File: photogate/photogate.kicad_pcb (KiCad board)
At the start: 2 copper layers, 72.8 x 62.1 mm, 21 parts, among them P2 3poles LOGO, P2 Jack F SJ1-3525N

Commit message: att designe PCB
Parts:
- removed Inferior Esquerdo: MountingHole_2.2mm_M2, MountingHole:MountingHole_2.2mm_M2
- removed P2 Jack F: SJ1-3525N, MyFootprints:CUI_SJ1-3525N
- removed REF** (x3): MountingHole_2.2mm_M2, MountingHole:MountingHole_2.2mm_M2
- removed REF**: OSHW-Logo_11.4x12mm_SilkScreen, Symbol:OSHW-Logo_11.4x12mm_SilkScreen
- added Furo Central: MountingHole_2.2mm_M2, MountingHole:MountingHole_2.2mm_M2, F.Cu at (110.1, 91.4)
- added Furo Inferior1: MountingHole_2.2mm_M2, MountingHole:MountingHole_2.2mm_M2, F.Cu at (94.8, 127.0)
- added Furo Inferior2: MountingHole_2.2mm_M2, MountingHole:MountingHole_2.2mm_M2, F.Cu at (162.6, 127.0)
- added Furo Superior: MountingHole_2.2mm_M2, MountingHole:MountingHole_2.2mm_M2, F.Cu at (162.6, 81.3)
- added P2 jack: SJ1-3515N, MyFootprints:CUI_SJ1-3515N, F.Cu at (91.6, 93.1)
- added R5: 470, Resistor_THT:R_Axial_DIN0204_L3.6mm_D1.6mm_P7.62mm_Horizontal, F.Cu at (104.3, 104.3)
- C1: value 104 -> 104k; footprint Capacitor_THT:C_Disc_D5.1mm_W3.2mm_P5.00mm -> Capacitor_THT:C_Disc_D10.5mm_W5.0mm_P10.00mm
- DC-005: renamed from Jack 5V1
- GLed: renamed from Green Led
- LM393N: value LM393N_A -> LM393N1
- R1: renamed from R4; footprint Resistor_THT:R_Axial_DIN0204_L3.6mm_D1.6mm_P5.08mm_Horizontal -> Resistor_THT:R_Axial_DIN0204_L3.6mm_D1.6mm_P7.62mm_Horizontal
- R2: renamed from R3; footprint Resistor_THT:R_Axial_DIN0204_L3.6mm_D1.6mm_P5.08mm_Horizontal -> Resistor_THT:R_Axial_DIN0204_L3.6mm_D1.6mm_P7.62mm_Horizontal
- R3: renamed from R1; footprint Resistor_THT:R_Axial_DIN0204_L3.6mm_D1.6mm_P5.08mm_Horizontal -> Resistor_THT:R_Axial_DIN0204_L3.6mm_D1.6mm_P7.62mm_Horizontal
- R4: renamed from R2; footprint Resistor_THT:R_Axial_DIN0204_L3.6mm_D1.6mm_P5.08mm_Horizontal -> Resistor_THT:R_Axial_DIN0204_L3.6mm_D1.6mm_P7.62mm_Horizontal
- RLed: renamed from Red Led
- moved P2 3poles 30.0 mm to (102.0, 101.2)
- moved R4 28.5 mm to (103.5, 107.7), turned to -90 degrees
- moved C1 22.8 mm to (119.4, 109.7), turned to -90 degrees
- moved R2 21.8 mm to (125.5, 79.5)
- moved DC-005 21.1 mm to (96.0, 77.7)
- moved VR1 18.9 mm to (94.6, 112.8), turned to -90 degrees
- moved R1 13.3 mm to (136.8, 79.5)
- moved R3 13.3 mm to (107.0, 78.7), turned to -90 degrees
- moved LM393N 12.9 mm to (110.6, 114.8)
- moved GLed 12.3 mm to (143.8, 72.0)
- moved RLed 12.3 mm to (132.4, 72.0)
- moved Encoder 12.3 mm to (121.0, 72.0)
- moved Display 12.3 mm to (160.2, 72.0)
- moved UFPR 11.1 mm to (158.7, 100.8)
- moved Esp32 DevKit V1 9.32 mm to (137.0, 87.0)
- renumbered VR to VR1
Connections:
- DC-005 pad 4: Net-(C1-Pad1) -> Net-(Esp32-Pad15)
- Display pad 2: Net-(C1-Pad1) -> Net-(Esp32-Pad15)
- Encoder pad 2: Net-(C1-Pad1) -> Net-(Esp32-Pad15)
- Esp32 DevKit V1 pad 15: Net-(C1-Pad1) -> Net-(Esp32-Pad15)
- Esp32 DevKit V1 pad 16: unconnected-(Esp32-Pad16) -> Net-(C1-Pad1)
- Esp32 DevKit V1 pad 17: unconnected-(Esp32-Pad17) -> GND
- R2 pad 2: Net-(C1-Pad1) -> Net-(R2-Pad2)
- R3 pad 1: Net-(C1-Pad1) -> Net-(Esp32-Pad15)
- RLed pad 2: /D0 -> Net-(R2-Pad2)
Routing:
- net Net-(Esp32-Pad15): track 0.00 -> 113.2 mm
- net GND: track 143.7 -> 214.2 mm
- net Net-(C1-Pad1): track 114.5 -> 68.7 mm
- net /PHOTODIODE: track 60.8 -> 30.5 mm
- net /D0: track 59.0 -> 43.7 mm
- net Net-(R2-Pad2): track 0.00 -> 4.29 mm
- net /DT: track 23.0 -> 27.1 mm
- net /SW: track 19.5 -> 23.5 mm
- net /CLK: track 26.6 -> 30.7 mm
- net Net-(P2jack1-Pad3): track 7.22 -> 11.1 mm
- net Net-(Esp32-Pad6): track 27.6 -> 25.3 mm
- net Net-(LM393N_A1-Pad2): track 11.2 -> 9.61 mm
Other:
- board size 72.8 x 62.1 mm -> 77.9 x 64 mm
- board text added: "Feito por: Marcio Ap. Bulla Jr. Orientado pelo: Fabiano Yokaichiya Código Fonte: github.com/MarcioBulla/Cronometro-Optico"
- board text removed: "Feito por: Marcio Ap. Bulla Jr. Código Fonte: github.com/MarcioBulla/Cronometro-Optico"

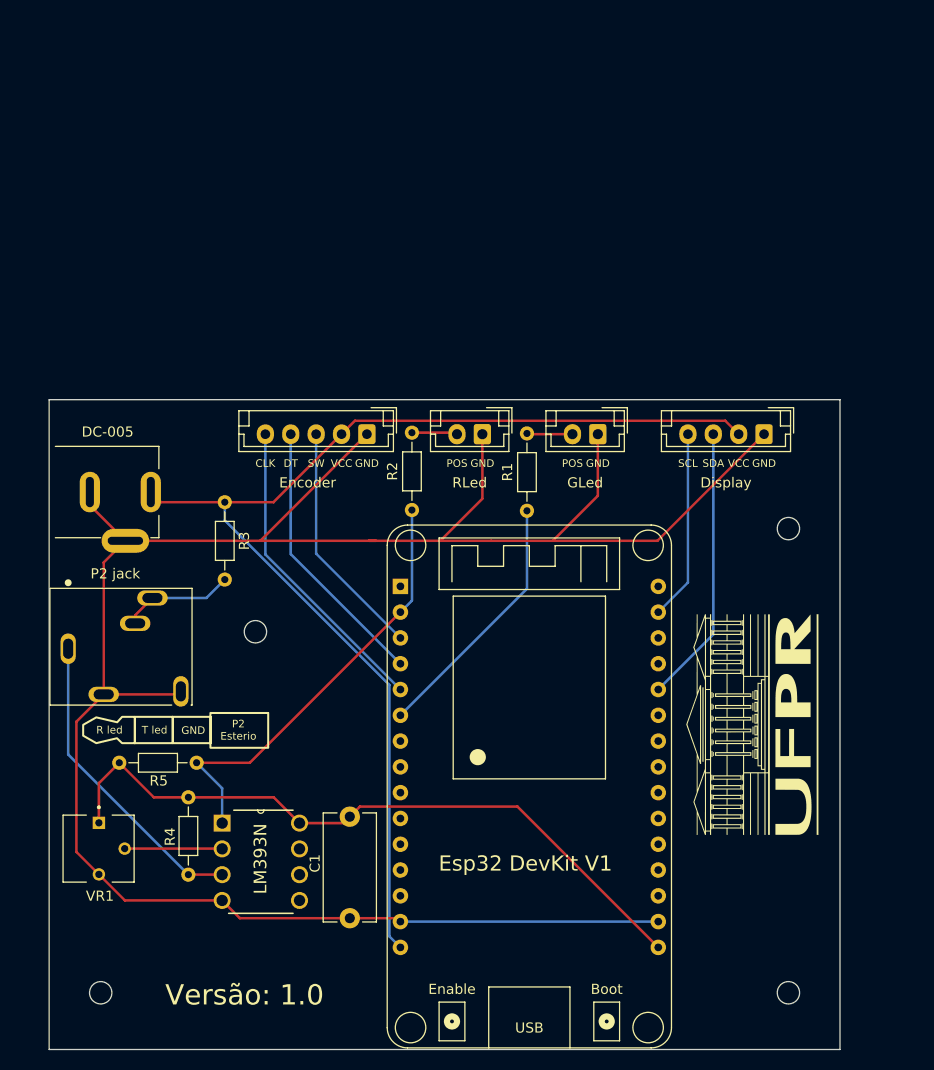
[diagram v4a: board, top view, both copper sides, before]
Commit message: Add connector para switch
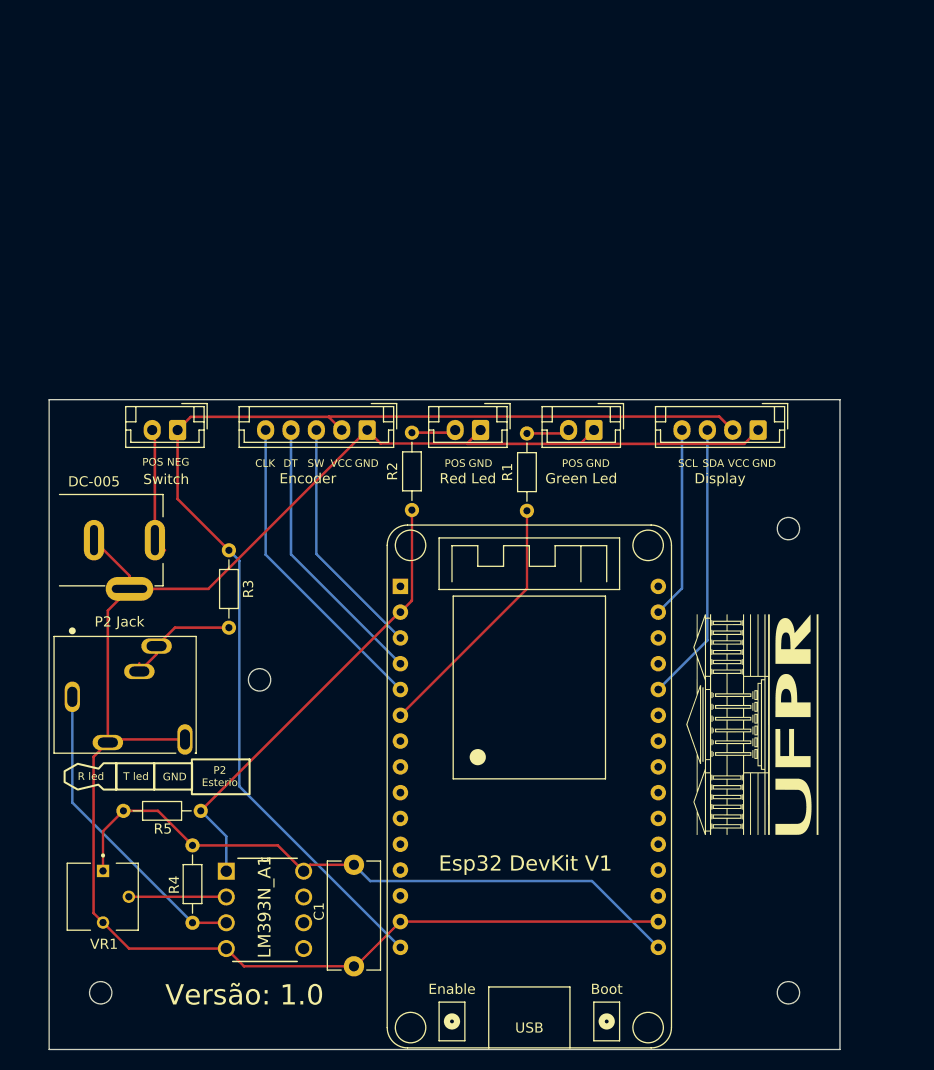
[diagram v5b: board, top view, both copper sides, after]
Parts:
- added Switch: Conn_01x02_Female, Connector_JST:JST_EH_B2B-EH-A_1x02_P2.50mm_Vertical, F.Cu at (102.4, 71.6)
- Green Led: renamed from GLed
- P2 Jack: renamed from P2 jack
- R5: value 470 -> 100
- Red Led: renamed from RLed
- moved P2 3poles 4.92 mm to (100.2, 105.8)
- moved R4 4.76 mm to (103.9, 112.5)
- moved P2 Jack 4.76 mm to (92.0, 97.9)
- moved R5 4.76 mm to (104.7, 109.1)
- moved C1 4.76 mm to (119.8, 114.4)
- moved DC-005 4.76 mm to (96.4, 82.4)
- moved Furo Central 4.76 mm to (110.5, 96.2)
- moved LM393N_A1 4.76 mm to (111.0, 119.5)
- moved R3 4.76 mm to (107.4, 83.4)
- moved VR1 4.76 mm to (95.0, 117.5)
- moved Display 0.71 mm to (159.6, 71.6)
- moved Green Led 0.56 mm to (143.4, 71.6)
- moved Red Led 0.45 mm to (132.2, 71.6)
- moved Encoder 0.41 mm to (121.1, 71.6)
- renumbered LM393N to LM393N_A1
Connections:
- DC-005 pad 4: Net-(Esp32-Pad15) -> Net-(switch1-Pad2)
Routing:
- net GND: track 214.2 -> 182.9 mm
- net Net-(switch1-Pad2): track 0.00 -> 12.4 mm
- net Net-(Esp32-Pad15): track 113.2 -> 117.7 mm
- net /D0: track 43.7 -> 45.3 mm
- net Net-(C1-Pad1): track 68.7 -> 67.3 mm
- net Net-(P2jack1-Pad3): track 11.1 -> 11.9 mm
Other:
- board text added: "NEG"

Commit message: Trocar connector jst para KK
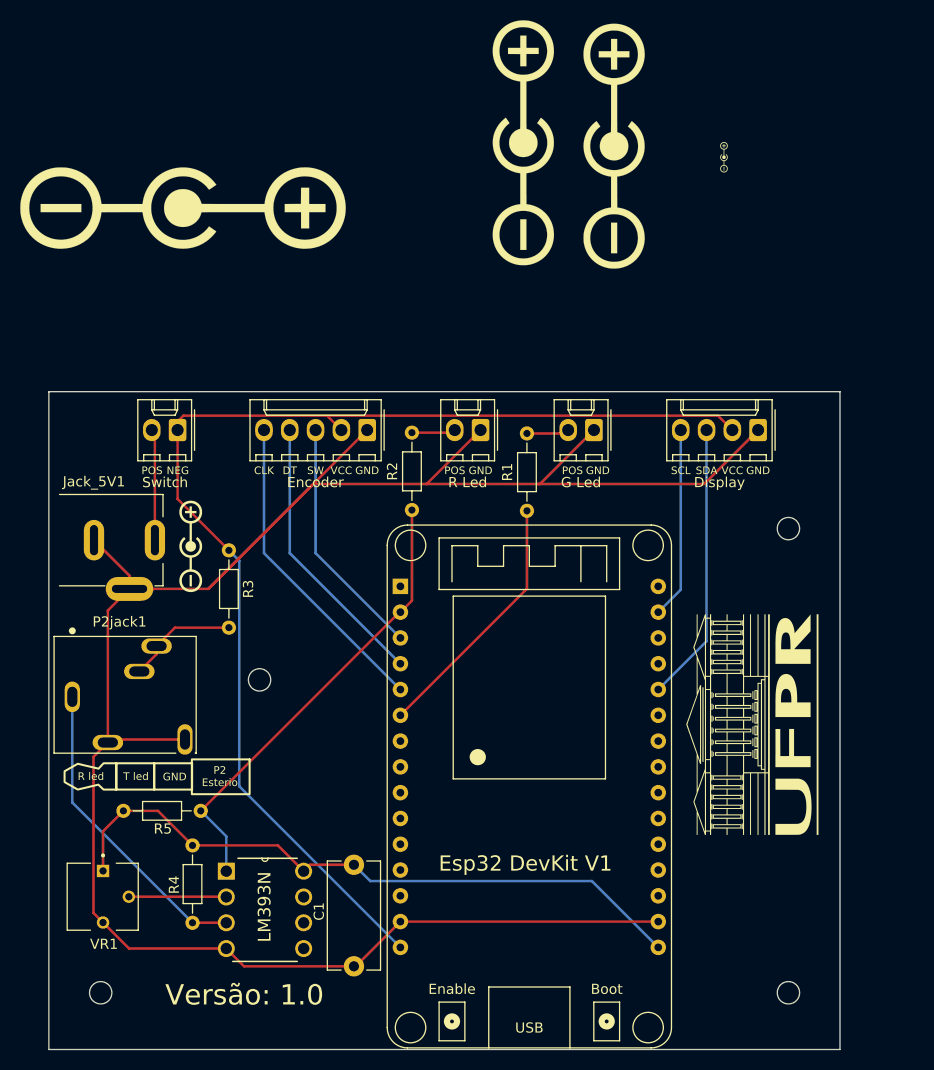
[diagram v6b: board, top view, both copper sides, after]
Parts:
- added REF**: Polarity_Center_Positive_6mm_SilkScreen, Symbol:Polarity_Center_Positive_6mm_SilkScreen, F.Cu at (136.4, 43.3)
- added REF**: Polarity_Center_Positive_6mm_SilkScreen, Symbol:Polarity_Center_Positive_6mm_SilkScreen, F.Cu at (145.4, 43.6)
- added REF**: Polarity_Center_Positive_8mm_SilkScreen, Symbol:Polarity_Center_Positive_8mm_SilkScreen, F.Cu at (102.9, 49.7)
- added polarity: Symbol, simbolos:Polarity_Center_Positive_9mm_SilkScreen, F.Cu at (103.7, 83.0)
- added symbol: LOGO, simbolos:Polarity_Center_Positive_3mm_SilkScreen, F.Cu at (156.2, 44.7)
- Display: footprint Connector_JST:JST_EH_B4B-EH-A_1x04_P2.50mm_Vertical -> Connector_Molex:Molex_KK-254_AE-6410-04A_1x04_P2.54mm_Vertical
- Encoder: footprint Connector_JST:JST_EH_B5B-EH-A_1x05_P2.50mm_Vertical -> Connector_Molex:Molex_KK-254_AE-6410-05A_1x05_P2.54mm_Vertical
- G Led: renamed from Green Led; footprint Connector_JST:JST_EH_B2B-EH-A_1x02_P2.50mm_Vertical -> Connector_Molex:Molex_KK-254_AE-6410-02A_1x02_P2.54mm_Vertical
- P2jack1: renamed from P2 Jack
- R Led: renamed from Red Led; footprint Connector_JST:JST_EH_B2B-EH-A_1x02_P2.50mm_Vertical -> Connector_Molex:Molex_KK-254_AE-6410-02A_1x02_P2.54mm_Vertical
- Switch: footprint Connector_JST:JST_EH_B2B-EH-A_1x02_P2.50mm_Vertical -> Connector_Molex:Molex_KK-254_AE-6410-02A_1x02_P2.54mm_Vertical
- renumbered DC-005 to Jack_5V1, LM393N_A1 to LM393N
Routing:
- net GND: track 182.9 -> 212.6 mm
- net Net-(C1-Pad1): track 67.3 -> 65.5 mm
- net Net-(Jack_5V1-Pad4): track 12.4 -> 11.3 mm
- net Net-(P2jack1-Pad3): track 11.9 -> 11.1 mm
- net Net-(Esp32-Pad15): track 117.7 -> 118.4 mm
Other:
- board size 77.9 x 64 mm -> 77.9 x 64.8 mm

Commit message: Ultimos ajustes
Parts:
- removed REF** (x2): Polarity_Center_Positive_6mm_SilkScreen, Symbol:Polarity_Center_Positive_6mm_SilkScreen
- removed REF**: Polarity_Center_Positive_8mm_SilkScreen, Symbol:Polarity_Center_Positive_8mm_SilkScreen
- removed symbol: LOGO, simbolos:Polarity_Center_Positive_3mm_SilkScreen
- Jack DC005: renamed from Jack_5V1
- jack P2 Stereo: renamed from P2jack1
- moved R3 1.77 mm to (107.4, 85.2)
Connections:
- R3 pad 2: Net-(P2jack1-Pad3) -> Net-(R3-Pad2)
- jack P2 Stereo pad 1: /PHOTODIODE -> GND
- jack P2 Stereo pad 2: GND -> /PHOTODIODE
- jack P2 Stereo pad 3: Net-(P2jack1-Pad3) -> Net-(R3-Pad2)
- jack P2 Stereo pad 4: GND -> unconnected-(P2jack1-Pad4)
- jack P2 Stereo pad 5: Net-(P2jack1-Pad3) -> unconnected-(P2jack1-Pad5)
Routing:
- net GND: track 212.6 -> 190.2 mm
- net Net-(P2jack1-Pad3): track 11.1 -> 0.00 mm
- net Net-(R3-Pad2): track 0.00 -> 7.14 mm
- net Net-(C1-Pad1): track 65.5 -> 70.2 mm
- net /PHOTODIODE: track 30.5 -> 29.2 mm
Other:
- board text added: "P2 Stereo"
- board text removed: "P2 Esterio"
